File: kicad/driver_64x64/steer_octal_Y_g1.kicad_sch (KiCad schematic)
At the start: 66 parts

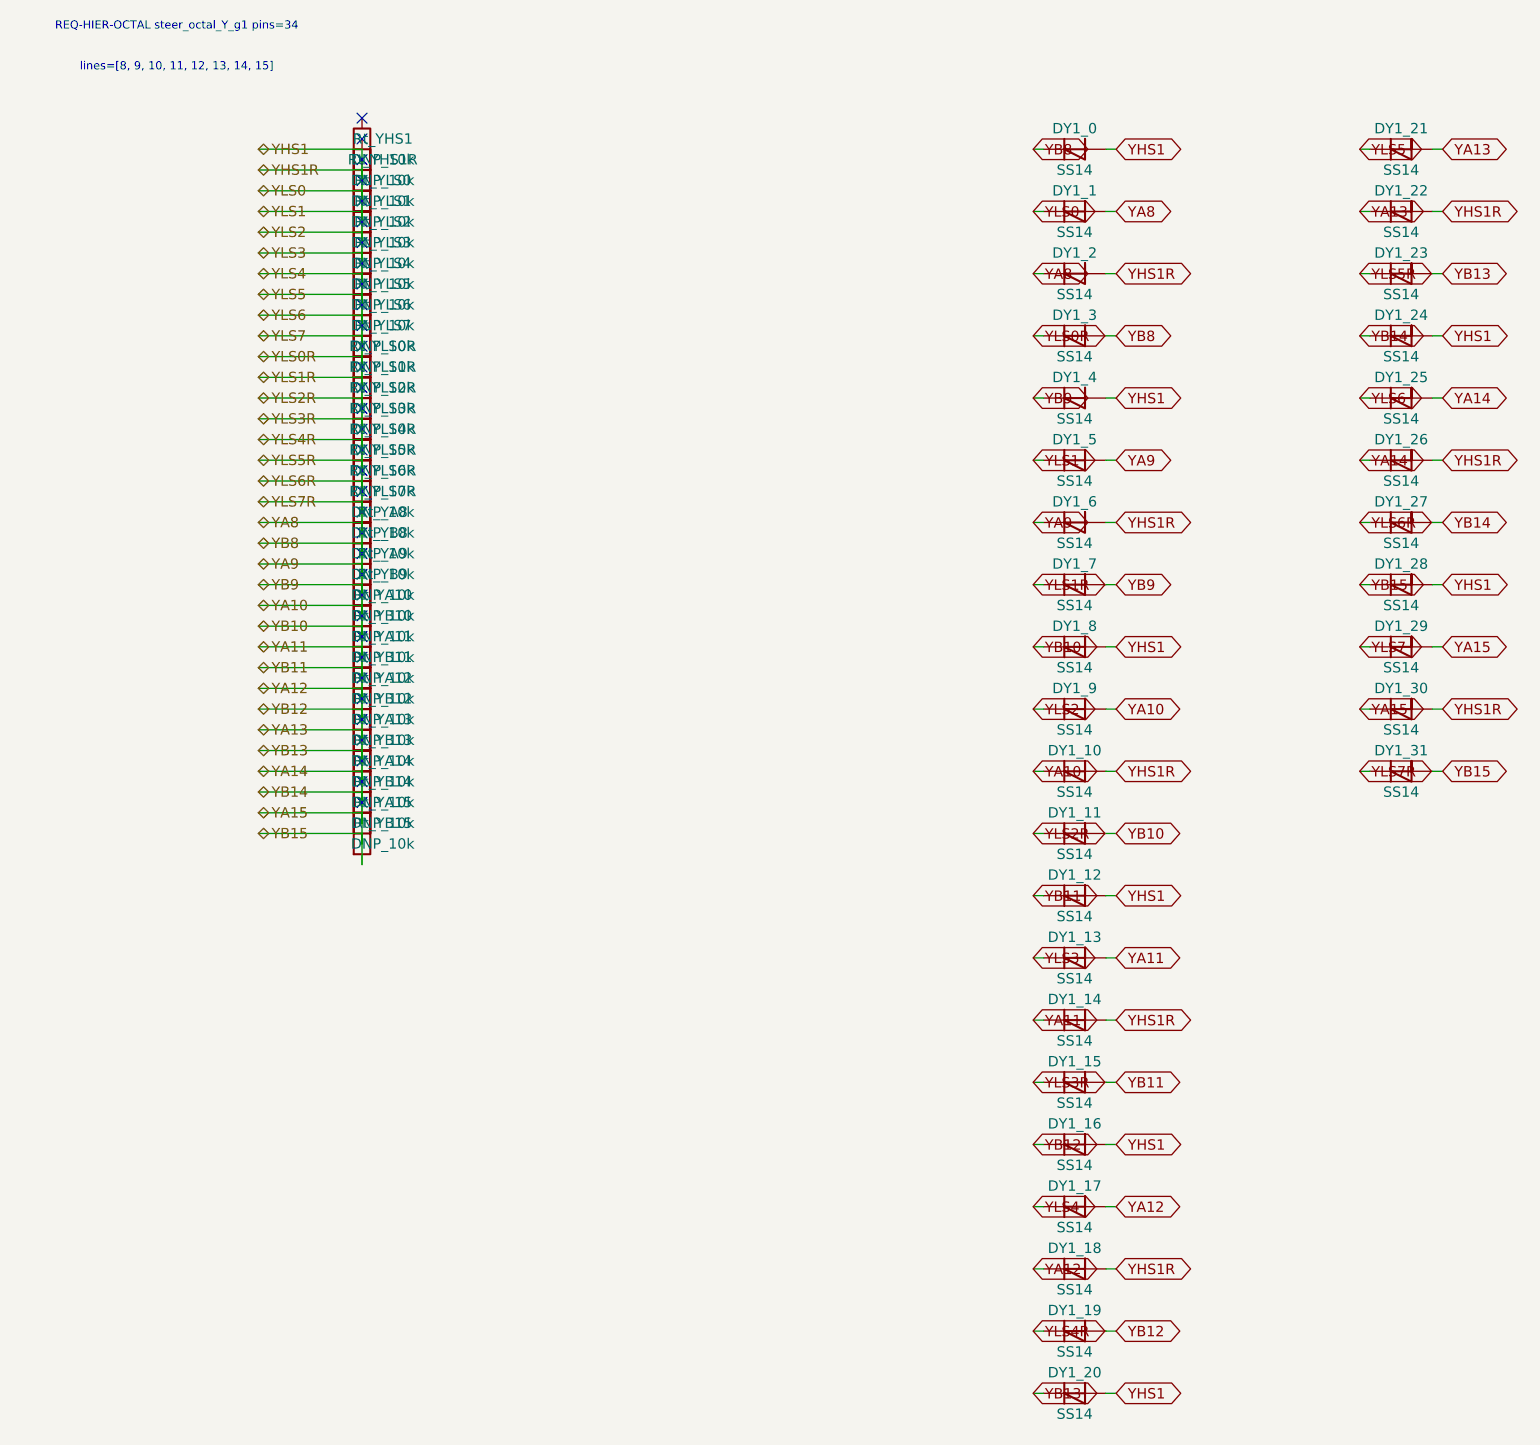
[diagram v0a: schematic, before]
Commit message: logical seperation into host and multiple decode/drive/steering boards
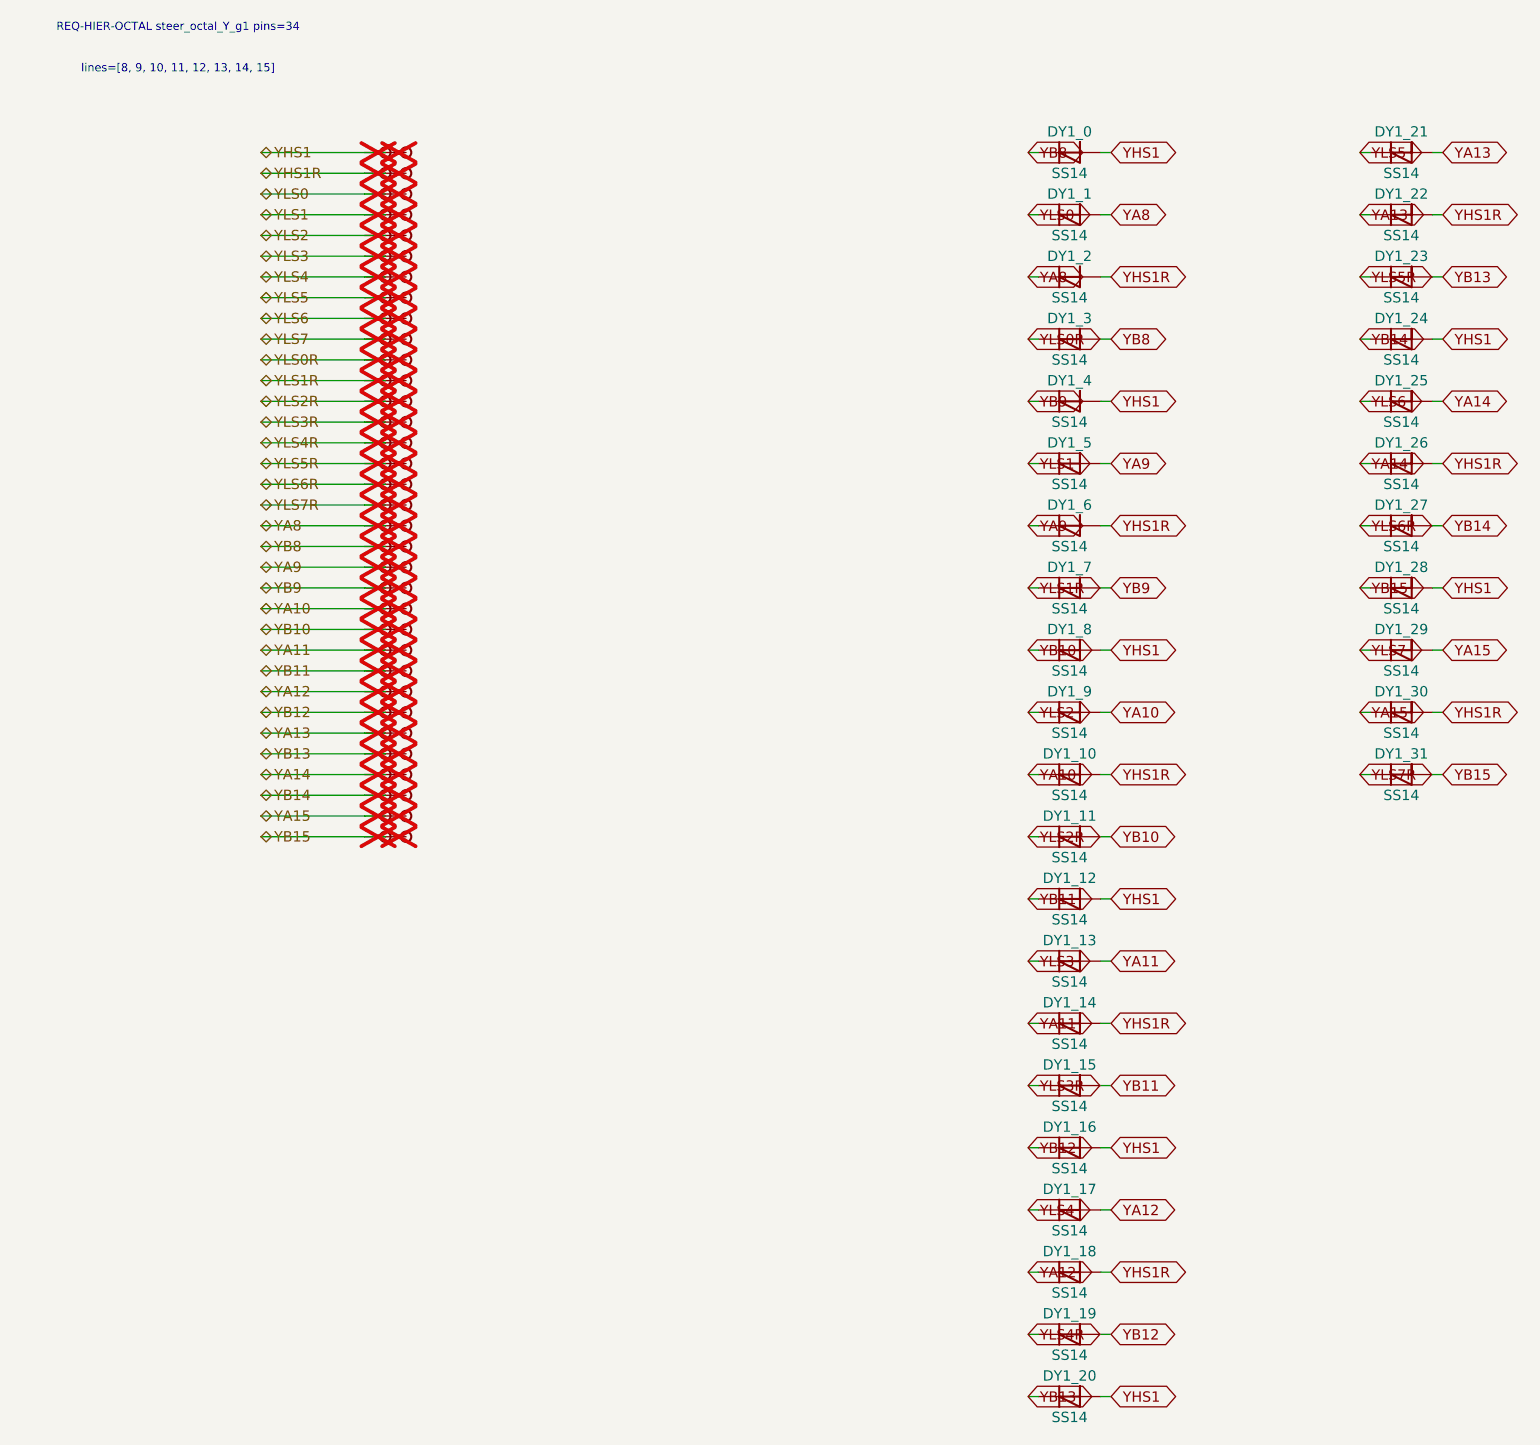
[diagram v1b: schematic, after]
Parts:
- removed Rt_YA10, Rt_YA11, Rt_YA12, Rt_YA13, Rt_YA14, Rt_YA15, Rt_YA8, Rt_YA9, Rt_YB10, Rt_YB11, Rt_YB12, Rt_YB13, Rt_YB14, Rt_YB15, Rt_YB8, Rt_YB9, Rt_YHS1, Rt_YHS1R, Rt_YLS0, Rt_YLS0R, Rt_YLS1, Rt_YLS1R, Rt_YLS2, Rt_YLS2R, Rt_YLS3, Rt_YLS3R, Rt_YLS4, Rt_YLS4R, Rt_YLS5, Rt_YLS5R, Rt_YLS6, Rt_YLS6R, Rt_YLS7, Rt_YLS7R: DNP_10k, symbol Device:R
- added TP_YA10, TP_YA10b, TP_YA11, TP_YA11b, TP_YA12, TP_YA12b, TP_YA13, TP_YA13b, TP_YA14, TP_YA14b, TP_YA15, TP_YA15b, TP_YA8, TP_YA8b, TP_YA9, TP_YA9b, TP_YB10, TP_YB10b, TP_YB11, TP_YB11b, TP_YB12, TP_YB12b, TP_YB13, TP_YB13b, TP_YB14, TP_YB14b, TP_YB15, TP_YB15b, TP_YB8, TP_YB8b, TP_YB9, TP_YB9b, TP_YHS1, TP_YHS1R, TP_YHS1Rb, TP_YHS1b, TP_YLS0, TP_YLS0R, TP_YLS0Rb, TP_YLS0b, TP_YLS1, TP_YLS1R, TP_YLS1Rb, TP_YLS1b, TP_YLS2, TP_YLS2R, TP_YLS2Rb, TP_YLS2b, TP_YLS3, TP_YLS3R, TP_YLS3Rb, TP_YLS3b, TP_YLS4, TP_YLS4R, TP_YLS4Rb, TP_YLS4b, TP_YLS5, TP_YLS5R, TP_YLS5Rb, TP_YLS5b, TP_YLS6, TP_YLS6R, TP_YLS6Rb, TP_YLS6b, TP_YLS7, TP_YLS7R, TP_YLS7Rb, TP_YLS7b: Stub, symbol CMR:Stub
- DY1_0, DY1_1, DY1_10, DY1_11, DY1_12, DY1_13, DY1_14, DY1_15, DY1_16, DY1_17, DY1_18, DY1_19, DY1_2, DY1_20, DY1_21, DY1_22, DY1_23, DY1_24, DY1_25, DY1_26, DY1_27, DY1_28, DY1_29, DY1_3, DY1_30, DY1_31, DY1_4, DY1_5, DY1_6, DY1_7, DY1_8, DY1_9: symbol Device:D_Schottky -> CMR:D_Schottky
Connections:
- net YA10: now also TP_YA10.1, TP_YA10b.1; no longer DY1_0.1 (K), DY1_0.2 (A), DY1_1.1 (K), DY1_1.2 (A), DY1_10.2 (A), DY1_11.1 (K), DY1_11.2 (A), DY1_12.1 (K), DY1_12.2 (A), DY1_13.1 (K), DY1_13.2 (A), DY1_14.1 (K), DY1_14.2 (A), DY1_15.1 (K), DY1_15.2 (A), DY1_16.1 (K), DY1_16.2 (A), DY1_17.1 (K), DY1_17.2 (A), DY1_18.1 (K), DY1_18.2 (A), DY1_19.1 (K), DY1_19.2 (A), DY1_2.1 (K), DY1_2.2 (A), DY1_20.1 (K), DY1_20.2 (A), DY1_21.1 (K), DY1_21.2 (A), DY1_22.1 (K), DY1_22.2 (A), DY1_23.1 (K), DY1_23.2 (A), DY1_24.1 (K), DY1_24.2 (A), DY1_25.1 (K), DY1_25.2 (A), DY1_26.1 (K), DY1_26.2 (A), DY1_27.1 (K), DY1_27.2 (A), DY1_28.1 (K), DY1_28.2 (A), DY1_29.1 (K), DY1_29.2 (A), DY1_3.1 (K), DY1_3.2 (A), DY1_30.1 (K), DY1_30.2 (A), DY1_31.1 (K), DY1_31.2 (A), DY1_4.1 (K), DY1_4.2 (A), DY1_5.1 (K), DY1_5.2 (A), DY1_6.1 (K), DY1_6.2 (A), DY1_7.1 (K), DY1_7.2 (A), DY1_8.1 (K), DY1_8.2 (A), DY1_9.1 (K)
- new net YA11: DY1_13.2 (A), DY1_14.1 (K), TP_YA11.1, TP_YA11b.1
- new net YA12: DY1_17.2 (A), DY1_18.1 (K), TP_YA12.1, TP_YA12b.1
- new net YA13: DY1_21.2 (A), DY1_22.1 (K), TP_YA13.1, TP_YA13b.1
- new net YA14: DY1_25.2 (A), DY1_26.1 (K), TP_YA14.1, TP_YA14b.1
- new net YA15: DY1_29.2 (A), DY1_30.1 (K), TP_YA15.1, TP_YA15b.1
- new net YA8: DY1_1.2 (A), DY1_2.1 (K), TP_YA8.1, TP_YA8b.1
- new net YA9: DY1_5.2 (A), DY1_6.1 (K), TP_YA9.1, TP_YA9b.1
- new net YB10: DY1_11.2 (A), DY1_8.1 (K), TP_YB10.1, TP_YB10b.1
- new net YB11: DY1_12.1 (K), DY1_15.2 (A), TP_YB11.1, TP_YB11b.1
- new net YB12: DY1_16.1 (K), DY1_19.2 (A), TP_YB12.1, TP_YB12b.1
- new net YB13: DY1_20.1 (K), DY1_23.2 (A), TP_YB13.1, TP_YB13b.1
- new net YB14: DY1_24.1 (K), DY1_27.2 (A), TP_YB14.1, TP_YB14b.1
- new net YB15: DY1_28.1 (K), DY1_31.2 (A), TP_YB15.1, TP_YB15b.1
- new net YB8: DY1_0.1 (K), DY1_3.2 (A), TP_YB8.1, TP_YB8b.1
- new net YB9: DY1_4.1 (K), DY1_7.2 (A), TP_YB9.1, TP_YB9b.1
- new net YHS1: DY1_0.2 (A), DY1_12.2 (A), DY1_16.2 (A), DY1_20.2 (A), DY1_24.2 (A), DY1_28.2 (A), DY1_4.2 (A), DY1_8.2 (A), TP_YHS1.1, TP_YHS1b.1
- new net YHS1R: DY1_10.2 (A), DY1_14.2 (A), DY1_18.2 (A), DY1_2.2 (A), DY1_22.2 (A), DY1_26.2 (A), DY1_30.2 (A), DY1_6.2 (A), TP_YHS1R.1, TP_YHS1Rb.1
- new net YLS0: DY1_1.1 (K), TP_YLS0.1, TP_YLS0b.1
- new net YLS0R: DY1_3.1 (K), TP_YLS0R.1, TP_YLS0Rb.1
- new net YLS1: DY1_5.1 (K), TP_YLS1.1, TP_YLS1b.1
- new net YLS1R: DY1_7.1 (K), TP_YLS1R.1, TP_YLS1Rb.1
- new net YLS2: DY1_9.1 (K), TP_YLS2.1, TP_YLS2b.1
- new net YLS2R: DY1_11.1 (K), TP_YLS2R.1, TP_YLS2Rb.1
- new net YLS3: DY1_13.1 (K), TP_YLS3.1, TP_YLS3b.1
- new net YLS3R: DY1_15.1 (K), TP_YLS3R.1, TP_YLS3Rb.1
- new net YLS4: DY1_17.1 (K), TP_YLS4.1, TP_YLS4b.1
- new net YLS4R: DY1_19.1 (K), TP_YLS4R.1, TP_YLS4Rb.1
- new net YLS5: DY1_21.1 (K), TP_YLS5.1, TP_YLS5b.1
- new net YLS5R: DY1_23.1 (K), TP_YLS5R.1, TP_YLS5Rb.1
- new net YLS6: DY1_25.1 (K), TP_YLS6.1, TP_YLS6b.1
- new net YLS6R: DY1_27.1 (K), TP_YLS6R.1, TP_YLS6Rb.1
- new net YLS7: DY1_29.1 (K), TP_YLS7.1, TP_YLS7b.1
- new net YLS7R: DY1_31.1 (K), TP_YLS7R.1, TP_YLS7Rb.1
- no-connect marks 34 -> 0
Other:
- moved on the sheet: DY1_0, DY1_1, DY1_10, DY1_11, DY1_12, DY1_13, DY1_14, DY1_15, DY1_16, DY1_17, DY1_18, DY1_19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
